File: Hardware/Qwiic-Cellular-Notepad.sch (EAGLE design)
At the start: 57 parts, among them J10 U.FL, J12 U.FL, J14 I2C, J15 SIM Socket, J3 QWIIC_RIGHT_ANGLE, J6 External SIM, J8 QWIIC_RIGHT_ANGLE, U2 MCP73831, U4 BLUES NOTECARD

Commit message: Fix Notecard FP. Add VIO vreg. x02 release.
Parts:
- removed E1, E2: ANTENNA-GROUNDEDEDGE_SMA_SMD, SparkFun-RF:ANTENNA-GROUNDEDEDGE_SMA_SMD
- added C17, C18: 1.0uF, SparkFun-Capacitors:1.0UF-0603-16V-10%-X7R
- added E3, E4: SMA, SparkFun-RF:ANTENNA-SMA-GROUNDEDEDGE_SMA_SMD
- added U1: STLQ015-3.3V, SparkFun-IC-Power:STLQ015-3.3V
- H5: value STAND-OFF-REFLOW2.5MM_TALL -> STAND-OFF
- J15: device SparkFun-Connectors:SIMHOLDERSIM -> SparkFun-Connectors:SIMHOLDER-SIM
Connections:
- new net VIO: C18.1, U1.OUT, U4.VIO
- net GND: now also C17.2, C18.2, E3.GND, E4.GND, U1.GND; no longer E1.GND, E2.GND
- net RF_GPS: now also E4.SIGNAL; no longer E1.SIGNAL
- net RF_LTE: now also E3.SIGNAL; no longer E2.SIGNAL
- net VIN: now also C17.1, U1.EN, U1.IN; no longer U4.VIO
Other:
- note added: "150mA max/1uA Quiescent"
- note added: "Maintains GNSS data/almanac"
- note added: "VIO Regulator"
- note added: "x02"
- note removed: "v11"
- moved on the sheet: C5, C6, C7, C8, D1, D4, D5, D6, H5, MEAS, R11, VIN_LED

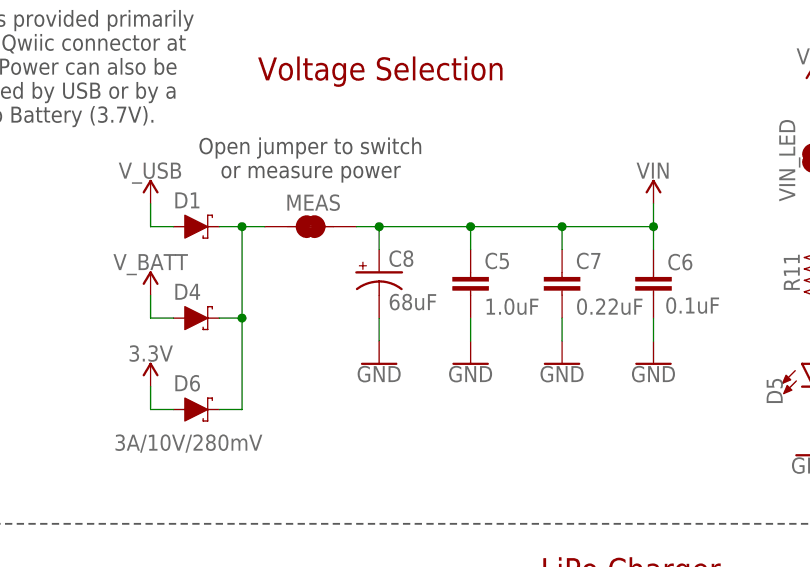
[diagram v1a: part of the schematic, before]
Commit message: Change to 22uF cap. Add production files.
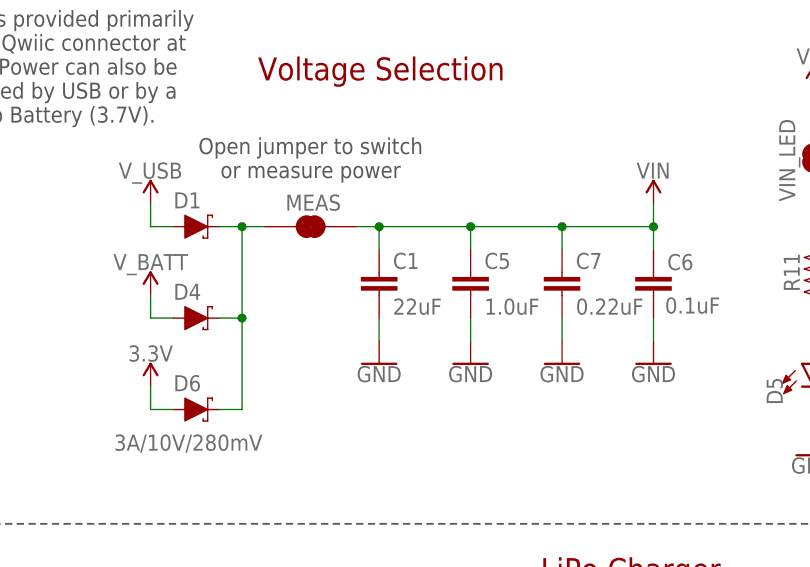
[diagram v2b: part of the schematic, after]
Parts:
- removed C8: 68uF, SparkFun-Capacitors:68UF-POLAR-EIA3528-10V-10%(TANT)
- added C1: 22uF, SparkFun-Capacitors:22UF-1210-16V-20%
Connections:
- net GND: now also C1.2; no longer C8.-
- net VIN: now also C1.1; no longer C8.+
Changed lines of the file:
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@@
 <part name="SUPPLY4" library="SparkFun-PowerSymbols" deviceset="V_USB" device=""/>
 <part name="J16" library="SparkFun-Connectors" deviceset="CONN_07" device="NO_SILK"/>
-<part name="C8" library="SparkFun-Capacitors" deviceset="68UF-POLAR" device="-EIA3528-10V-10%(TANT)" value="68uF"/>
 <part name="J2" library="SparkFun-Connectors" deviceset="CONN_02" device="1X02_NO_SILK"/>
 <part name="J5" library="SparkFun-Connectors" deviceset="CONN_10" device="NO_SILK_PTH_FEMALE"/>
@@
 <part name="GND49" library="SparkFun-PowerSymbols" deviceset="GND" device=""/>
 <part name="SUPPLY9" library="SparkFun-PowerSymbols" deviceset="VIN" device=""/>
+<part name="C1" library="SparkFun-Capacitors" deviceset="22UF" device="-1210-16V-20%" value="22uF"/>
 </parts>
 <sheets>
@@
 <attribute name="NAME" x="205.74" y="84.328" size="1.778" layer="95" font="vector" rot="MR0"/>
 </instance>
-<instance part="C8" gate="G$1" x="55.88" y="243.84" smashed="yes">
-<attribute name="NAME" x="56.896" y="244.475" size="1.778" layer="95" font="vector"/>
-<attribute name="VALUE" x="56.896" y="239.649" size="1.778" layer="96" font="vector"/>
-</instance>
 <instance part="J2" gate="G$1" x="203.2" y="53.34" smashed="yes" rot="MR0">
 <attribute name="VALUE" x="205.74" y="48.514" size="1.778" layer="96" font="vector" rot="MR0"/>
@@
 <instance part="SUPPLY9" gate="G$1" x="121.92" y="254" smashed="yes">
 <attribute name="VALUE" x="121.92" y="256.794" size="1.778" layer="96" align="bottom-center"/>
+</instance>
+<instance part="C1" gate="G$1" x="55.88" y="241.3" smashed="yes">
+<attribute name="NAME" x="57.404" y="244.221" size="1.778" layer="95" font="vector"/>
+<attribute name="VALUE" x="57.404" y="239.141" size="1.778" layer="96" font="vector"/>
 </instance>
 </instances>
@@
 </segment>
 <segment>
-<pinref part="C8" gate="G$1" pin="-"/>
 <wire x1="55.88" y1="238.76" x2="55.88" y2="236.22" width="0.1524" layer="91"/>
 <pinref part="GND17" gate="1" pin="GND"/>
+<pinref part="C1" gate="G$1" pin="2"/>
 </segment>
 <segment>
@@
 <pinref part="MEAS" gate="JP1" pin="2"/>
 <pinref part="SUPPLY1" gate="G$1" pin="VIN"/>
-<pinref part="C8" gate="G$1" pin="+"/>
 <wire x1="55.88" y1="246.38" x2="55.88" y2="248.92" width="0.1524" layer="91"/>
 <junction x="55.88" y="248.92"/>
-</segment>
-<segment>
+<pinref part="C1" gate="G$1" pin="1"/>
+</segment>
+<segment>

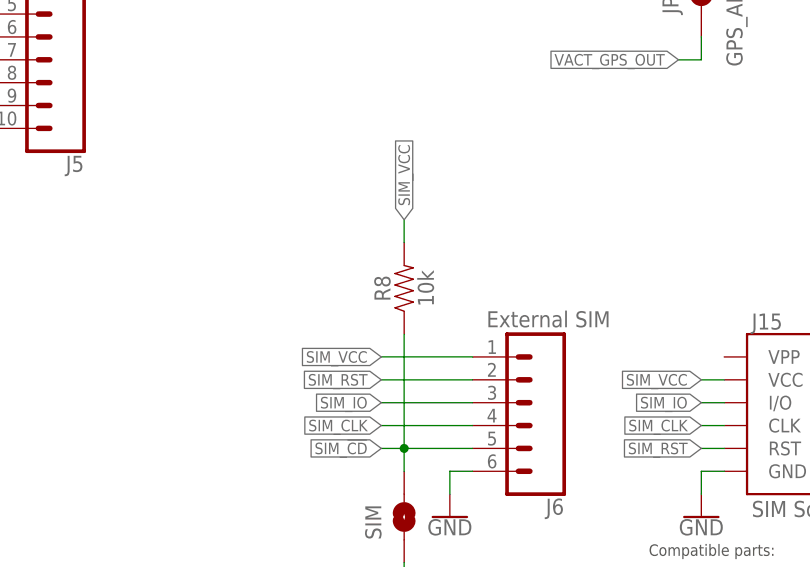
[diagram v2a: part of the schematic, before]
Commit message: Change R8 to DNP.
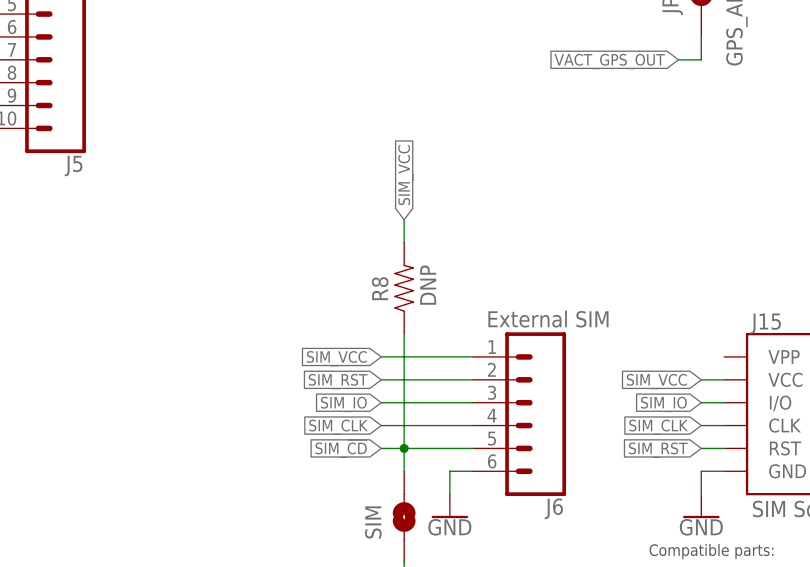
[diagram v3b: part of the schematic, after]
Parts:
- R8: value 10k -> DNP; device SparkFun-Resistors:10KOHM-0603-1/10W-1% -> Testing:RESISTOR0603-RES
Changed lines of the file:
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@@
 <part name="SUPPLY8" library="SparkFun-PowerSymbols" deviceset="3.3V" device=""/>
 <part name="J6" library="SparkFun-Connectors" deviceset="CONN_06" device="NO_SILK_NO_POP" value="External SIM"/>
-<part name="R8" library="SparkFun-Resistors" deviceset="10KOHM" device="-0603-1/10W-1%" value="10k"/>
+<part name="R8" library="Testing" deviceset="RESISTOR" device="0603-RES" value="DNP"/>
 <part name="GND25" library="SparkFun-PowerSymbols" deviceset="GND" device=""/>
 <part name="GND1" library="SparkFun-PowerSymbols" deviceset="GND" device=""/>
@@
 </instance>
 <instance part="R8" gate="G$1" x="264.16" y="40.64" smashed="yes" rot="R90">
-<attribute name="NAME" x="262.636" y="40.64" size="1.778" layer="95" font="vector" rot="R90" align="bottom-center"/>
-<attribute name="VALUE" x="265.684" y="40.64" size="1.778" layer="96" font="vector" rot="R90" align="top-center"/>
+<attribute name="NAME" x="262.382" y="39.116" size="1.778" layer="95" rot="R90"/>
+<attribute name="VALUE" x="267.716" y="38.608" size="1.778" layer="96" rot="R90"/>
 </instance>
 <instance part="GND25" gate="1" x="269.24" y="15.24" smashed="yes">
